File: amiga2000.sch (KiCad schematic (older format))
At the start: 0 parts

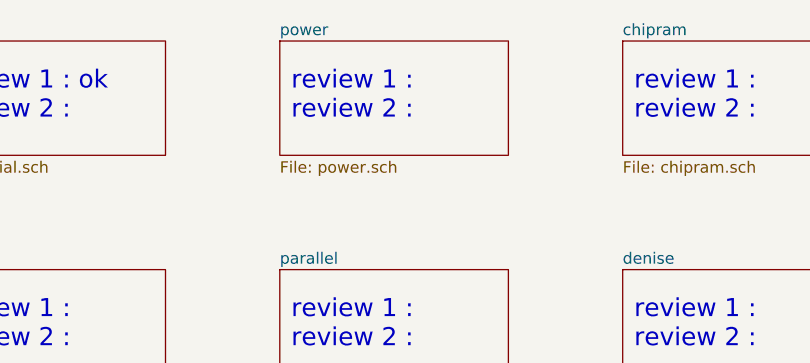
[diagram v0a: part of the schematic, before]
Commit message: Power review; Add missing mouting holes
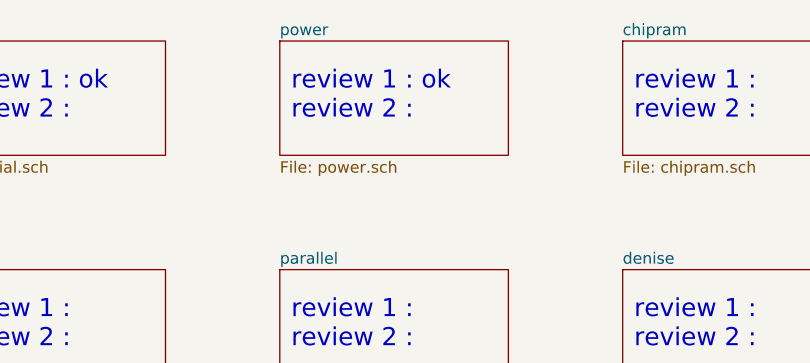
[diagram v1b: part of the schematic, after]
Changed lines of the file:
@@
 review 1 :\nreview 2 :
 Text Notes 5550 1350 0    79   ~ 0
-review 1 :\nreview 2 :
+review 1 : ok\nreview 2 :
 Text Notes 4050 1350 0    79   ~ 0
 review 1 : ok\nreview 2 :

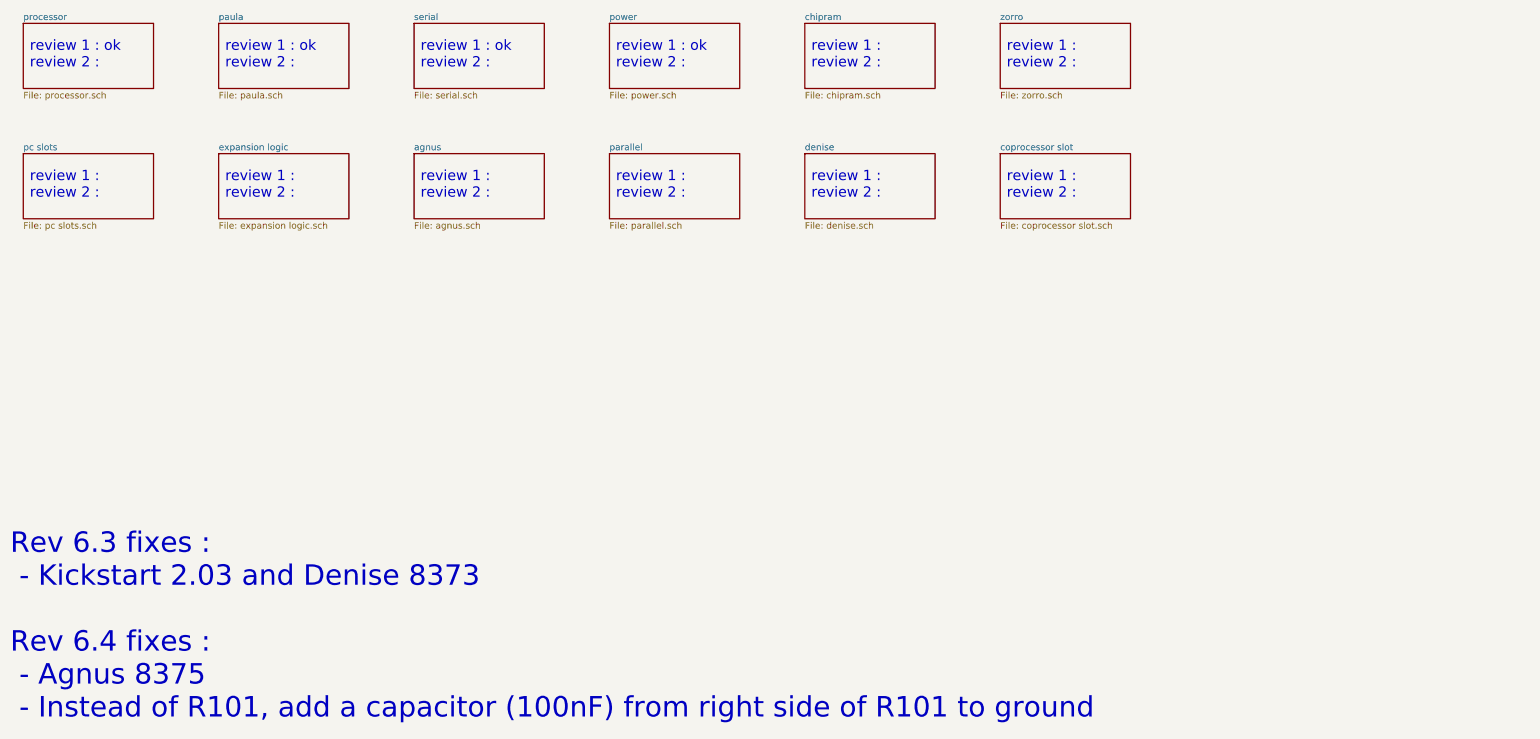
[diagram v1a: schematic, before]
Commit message: Spotted error in original scanned schematics
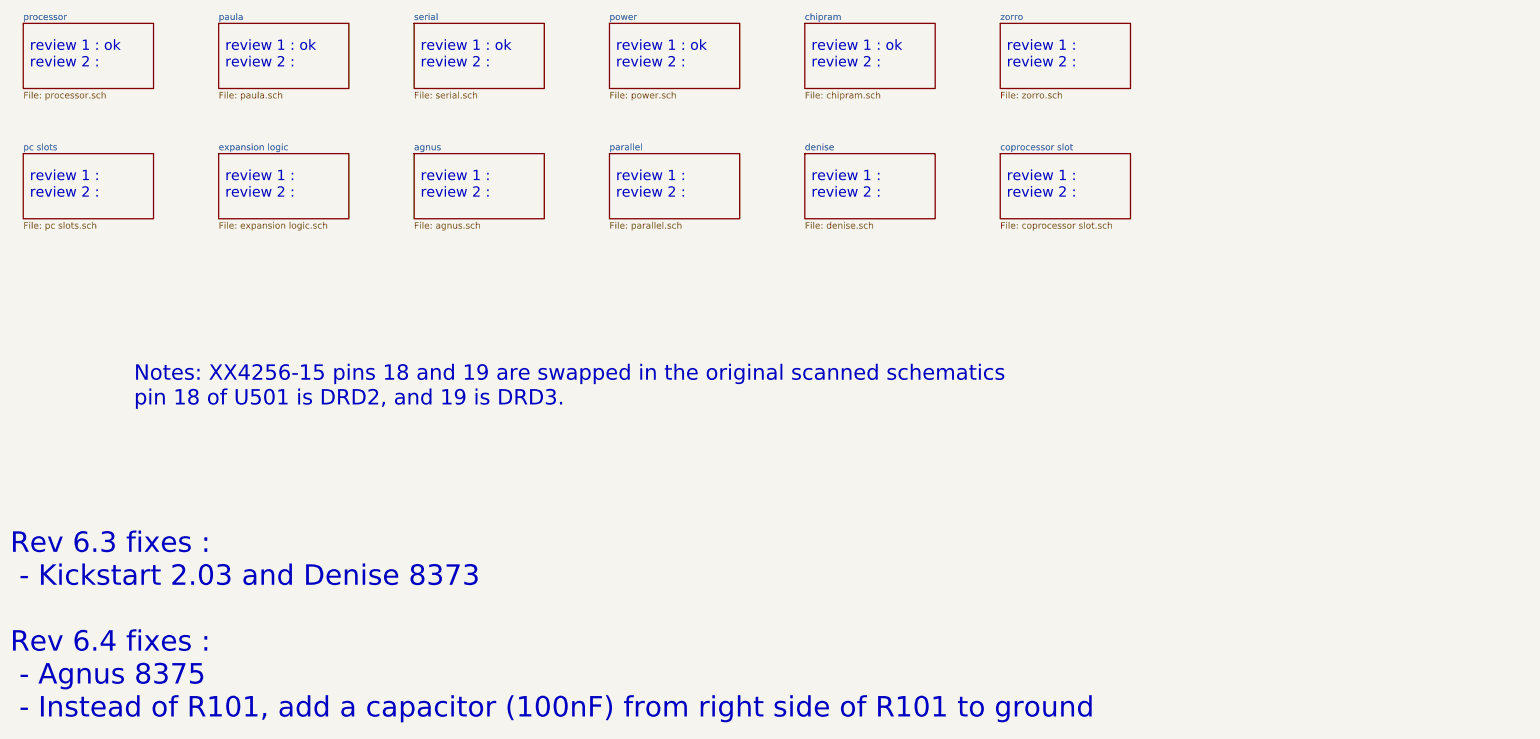
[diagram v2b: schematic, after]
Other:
- note added: "Notes: XX4256-15 pins 18 and 19 are swapped in the original scanned schematics\npin 18 of U501 is DRD2, and 19 is DRD3."
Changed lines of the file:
@@
 review 1 : ok\nreview 2 :
 Text Notes 7050 1350 0    79   ~ 0
-review 1 :\nreview 2 :
+review 1 : ok\nreview 2 :
 Text Notes 8550 1350 0    79   ~ 0
 review 1 :\nreview 2 :
@@
 Text Notes 7050 2350 0    79   ~ 0
 review 1 :\nreview 2 :
+Text Notes 1850 3950 0    118  ~ 0
+Notes: XX4256-15 pins 18 and 19 are swapped in the original scanned schematics\npin 18 of U501 is DRD2, and 19 is DRD3.
 $EndSCHEMATC

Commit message: One more review
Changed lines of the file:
@@
 review 1 : ok\nreview 2 :
 Text Notes 8550 1350 0    79   ~ 0
-review 1 :\nreview 2 :
+review 1 : ok\nreview 2 :
 Text Notes 8550 2350 0    79   ~ 0
 review 1 :\nreview 2 :

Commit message: more done
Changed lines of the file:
@@
 Rev 6.3 fixes :\n - Kickstart 2.03 and Denise 8373\n\nRev 6.4 fixes :\n - Agnus 8375\n - Instead of R101, add a capacitor (100nF) from right side of R101 to ground
 Text Notes 1050 2350 0    79   ~ 0
-review 1 :\nreview 2 :
+review 1 : ok\nreview 2 :
 Text Notes 2550 2350 0    79   ~ 0
-review 1 :\nreview 2 :
+review 1 : ok\nreview 2 :
 Text Notes 4050 2350 0    79   ~ 0
 review 1 :\nreview 2 :

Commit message: Review done
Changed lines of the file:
@@
 review 1 : ok\nreview 2 :
 Text Notes 4050 2350 0    79   ~ 0
-review 1 :\nreview 2 :
+review 1 : ok\nreview 2 :
 Text Notes 5550 2350 0    79   ~ 0
 review 1 :\nreview 2 :

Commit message: kbd ok
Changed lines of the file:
@@
 review 1 : ok\nreview 2 :
 Text Notes 8550 2350 0    79   ~ 0
-review 1 :\nreview 2 :
+review 1 : ok\nreview 2 :
 Text Notes 7050 2350 0    79   ~ 0
 review 1 :\nreview 2 :

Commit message: Review done
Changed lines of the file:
@@
 review 1 : ok\nreview 2 :
 Text Notes 5550 2350 0    79   ~ 0
-review 1 :\nreview 2 :
+review 1 : ok\nreview 2 :
 Text Notes 5550 1350 0    79   ~ 0
 review 1 : ok\nreview 2 :

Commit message: All reviews done
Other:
- note removed: "review 1 :\nreview 2 :"
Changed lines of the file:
@@
 review 1 : ok\nreview 2 :
 Text Notes 7050 2350 0    79   ~ 0
-review 1 :\nreview 2 :
+review 1 : ok\nreview 2 :
 Text Notes 1850 3950 0    118  ~ 0
 Notes: XX4256-15 pins 18 and 19 are swapped in the original scanned schematics\npin 18 of U501 is DRD2, and 19 is DRD3.
